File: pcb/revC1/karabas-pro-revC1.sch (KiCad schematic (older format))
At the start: 149 parts, among them CON1 CF-CARD, CON2 SD, CON3 VGA, CON4 Joystick, CON5 Keyboard, CON6 Mouse, CON7 Audio, CON8 5V DC, CON9 MicroSD', J1 Floppy, J2 FPGA JTAG, J3 Floppy, J4 uBus, J5 AVR JTAG, J6 AVR UART, SW1 SW_Push, SW2 SW_Push, SW3 Mode Selector, U1 EP4CE6E22C8N, U10 ESP-12E, U11 TDA1543, U12 AMS1117-3.3, U13 AMS1117-2.5, U14 AMS1117-1.2, U17 74LS06, U18 74LS38, U2 CY62167EV30, U3 M25P16, U4 EPM3128ATC100-5, U5 ATMEGA328-AU, U6 MB8877A, U7 TXB0104PW, U8 TXB0104PW, U9 DS1307Z+, X1 SG-7050CAN, Y1 32768Hz, Y2 16MHz

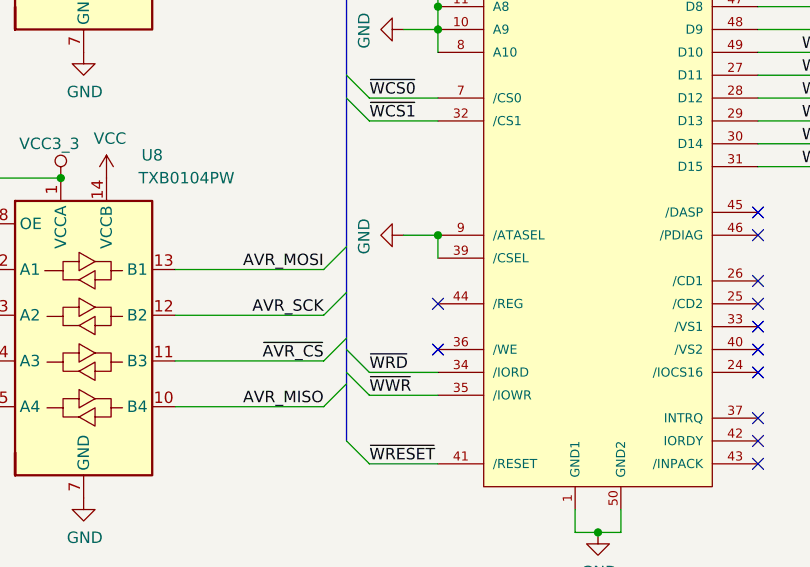
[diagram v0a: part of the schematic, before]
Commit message: Updated rev.C1: added CF card /REG pullup
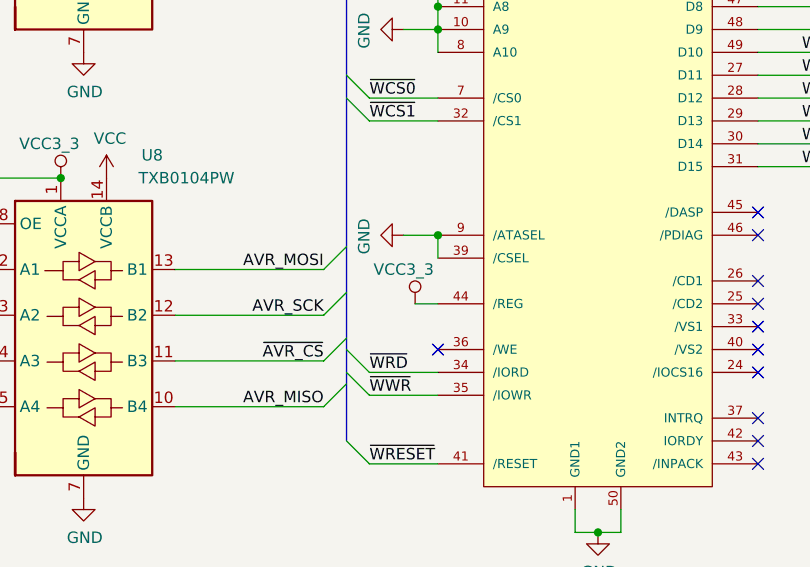
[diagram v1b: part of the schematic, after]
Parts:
- CON1: footprint footprints:TE_1734451-1 -> footprints:TE_1734451-1-LONG
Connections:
- net VCC3_3: now also CON1.44 (/REG)
- no-connect marks 60 -> 59
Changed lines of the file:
@@
 F 0 "CON1" H 9850 11931 50  0000 C CNN
 F 1 "CF-CARD" H 9850 11840 50  0000 C CNN
-F 2 "footprints:TE_1734451-1" H 9880 10300 20  0001 C CNN
+F 2 "footprints:TE_1734451-1-LONG" H 9880 10300 20  0001 C CNN
 F 3 "" H 9850 10150 60  0000 C CNN
 	1    9850 10150
@@
 	9150 10650 9150 10550
 Connection ~ 9150 10550
-NoConn ~ 9150 10850
 NoConn ~ 9150 11050
 Entry Wire Line
@@
 	1    0    0    -1
 $EndComp
-Wire Bus Line
-	14200 10200 14200 11000
-Wire Bus Line
-	14200 700  14200 10200
-Wire Bus Line
-	16000 4950 20350 4950
-Wire Bus Line
-	20350 4950 20350 10200
-Wire Bus Line
-	14200 10200 20350 10200
-Wire Bus Line
-	11050 700  11050 10150
-Wire Bus Line
-	4850 6350 4850 12550
-Wire Bus Line
-	3150 6350 3150 10550
-Wire Bus Line
-	700  6350 700  9700
-Wire Bus Line
-	700  700  6500 700
-Wire Bus Line
-	8750 700  8750 11450
-Wire Bus Line
-	6500 700  6500 11200
-Wire Bus Line
-	4850 6350 5350 6350
-Wire Bus Line
-	3150 6350 4850 6350
-Wire Bus Line
-	700  6350 3150 6350
-Wire Bus Line
-	700  700  700  6350
 Wire Wire Line
 	16550 10750 16950 10750
@@
 	15750 10750 16550 10750
 $Comp
-L vcc33:VCC3_3 #PWR?
+L vcc33:VCC3_3 #PWR0188
 U 1 1 5FD0478B
 P 17850 11550
-F 0 "#PWR?" H 17850 11400 50  0001 C CNN
+F 0 "#PWR0188" H 17850 11400 50  0001 C CNN
 F 1 "VCC3_3" H 17800 11700 50  0000 C CNN
 F 2 "" H 17850 11550 50  0001 C CNN
@@
 $EndComp
 $Comp
-L power:GND #PWR?
+L power:GND #PWR0189
 U 1 1 5FD04E19
 P 17850 11850
-F 0 "#PWR?" H 17850 11600 50  0001 C CNN
+F 0 "#PWR0189" H 17850 11600 50  0001 C CNN
 F 1 "GND" H 17855 11677 50  0000 C CNN
 F 2 "" H 17850 11850 50  0001 C CNN
@@
 	1    0    0    -1
 $EndComp
+$Comp
+L vcc33:VCC3_3 #PWR0190
+U 1 1 5FDAE6BE
+P 9050 10850
+F 0 "#PWR0190" H 9050 10700 50  0001 C CNN
+F 1 "VCC3_3" H 9000 11000 50  0000 C CNN
+F 2 "" H 9050 10850 50  0001 C CNN
+F 3 "" H 9050 10850 50  0001 C CNN
+	1    9050 10850
+	1    0    0    -1
+$EndComp
+Wire Wire Line
+	9050 10850 9150 10850
+Wire Bus Line
+	14200 10200 14200 11000
+Wire Bus Line
+	4850 6350 5350 6350
+Wire Bus Line
+	700  6350 3150 6350
+Wire Bus Line
+	3150 6350 3150 10550
+Wire Bus Line
+	700  6350 700  9700
+Wire Bus Line
+	3150 6350 4850 6350
+Wire Bus Line
+	700  700  700  6350
+Wire Bus Line
+	14200 10200 20350 10200
+Wire Bus Line
+	20350 4950 20350 10200
+Wire Bus Line
+	16000 4950 20350 4950
+Wire Bus Line
+	14200 700  14200 10200
+Wire Bus Line
+	4850 6350 4850 12550
+Wire Bus Line
+	700  700  6500 700
+Wire Bus Line
+	11050 700  11050 10150
+Wire Bus Line
+	6500 700  6500 11200
+Wire Bus Line
+	8750 700  8750 11450
 $EndSCHEMATC

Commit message: Grounded mounting holes and vga connector
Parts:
- CON3: symbol Connector:DB15_Female_HighDensity -> Connector:DB15_Female_HighDensity_MountingHoles
- H1, H2, H3, H4, H5, H6, H7, H8: symbol Mechanical:MountingHole -> Mechanical:MountingHole_Pad
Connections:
- net GND: now also CON3.0, H1.1, H2.1, H3.1, H4.1, H5.1, H6.1, H7.1, H8.1
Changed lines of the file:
@@
 $EndComp
 $Comp
-L Connector:DB15_Female_HighDensity CON3
+L Connector:DB15_Female_HighDensity_MountingHoles CON3
 U 1 1 5F338B53
 P 12650 1900
@@
 $EndComp
 $Comp
-L Mechanical:MountingHole H1
+L Mechanical:MountingHole_Pad H1
 U 1 1 5F34B048
-P 17550 14000
-F 0 "H1" H 17650 14046 50  0000 L CNN
-F 1 "MountingHole" H 17650 13955 50  0000 L CNN
-F 2 "MountingHole:MountingHole_3.5mm_Pad_Via" H 17550 14000 50  0001 C CNN
-F 3 "~" H 17550 14000 50  0001 C CNN
-	1    17550 14000
+P 14850 13950
+F 0 "H1" H 14950 13996 50  0000 L CNN
+F 1 "MountingHole" H 14950 13905 50  0000 L CNN
+F 2 "MountingHole:MountingHole_3.5mm_Pad_Via" H 14850 13950 50  0001 C CNN
+F 3 "~" H 14850 13950 50  0001 C CNN
+	1    14850 13950
 	1    0    0    -1
 $EndComp
 $Comp
-L Mechanical:MountingHole H2
+L Mechanical:MountingHole_Pad H2
 U 1 1 5F34C3F9
-P 17550 14200
-F 0 "H2" H 17650 14246 50  0000 L CNN
-F 1 "MountingHole" H 17650 14155 50  0000 L CNN
-F 2 "MountingHole:MountingHole_3.5mm_Pad_Via" H 17550 14200 50  0001 C CNN
-F 3 "~" H 17550 14200 50  0001 C CNN
-	1    17550 14200
+P 15550 13950
+F 0 "H2" H 15650 13996 50  0000 L CNN
+F 1 "MountingHole" H 15650 13905 50  0000 L CNN
+F 2 "MountingHole:MountingHole_3.5mm_Pad_Via" H 15550 13950 50  0001 C CNN
+F 3 "~" H 15550 13950 50  0001 C CNN
+	1    15550 13950
 	1    0    0    -1
 $EndComp
 $Comp
-L Mechanical:MountingHole H3
+L Mechanical:MountingHole_Pad H3
 U 1 1 5F34C76D
-P 17550 14400
-F 0 "H3" H 17650 14446 50  0000 L CNN
-F 1 "MountingHole" H 17650 14355 50  0000 L CNN
-F 2 "MountingHole:MountingHole_3.5mm_Pad_Via" H 17550 14400 50  0001 C CNN
-F 3 "~" H 17550 14400 50  0001 C CNN
-	1    17550 14400
+P 16250 13950
+F 0 "H3" H 16350 13996 50  0000 L CNN
+F 1 "MountingHole" H 16350 13905 50  0000 L CNN
+F 2 "MountingHole:MountingHole_3.5mm_Pad_Via" H 16250 13950 50  0001 C CNN
+F 3 "~" H 16250 13950 50  0001 C CNN
+	1    16250 13950
 	1    0    0    -1
 $EndComp
 $Comp
-L Mechanical:MountingHole H4
+L Mechanical:MountingHole_Pad H4
 U 1 1 5F34CA0C
-P 17550 14600
-F 0 "H4" H 17650 14646 50  0000 L CNN
-F 1 "MountingHole" H 17650 14555 50  0000 L CNN
-F 2 "MountingHole:MountingHole_3.5mm_Pad_Via" H 17550 14600 50  0001 C CNN
-F 3 "~" H 17550 14600 50  0001 C CNN
-	1    17550 14600
+P 16950 13950
+F 0 "H4" H 17050 13996 50  0000 L CNN
+F 1 "MountingHole" H 17050 13905 50  0000 L CNN
+F 2 "MountingHole:MountingHole_3.5mm_Pad_Via" H 16950 13950 50  0001 C CNN
+F 3 "~" H 16950 13950 50  0001 C CNN
+	1    16950 13950
 	1    0    0    -1
 $EndComp
@@
 $EndComp
 $Comp
-L Mechanical:MountingHole H5
+L Mechanical:MountingHole_Pad H5
 U 1 1 5ED90FCA
-P 17550 14950
-F 0 "H5" H 17650 14996 50  0000 L CNN
-F 1 "MountingHole" H 17650 14905 50  0000 L CNN
-F 2 "MountingHole:MountingHole_3.5mm_Pad_Via" H 17550 14950 50  0001 C CNN
-F 3 "~" H 17550 14950 50  0001 C CNN
-	1    17550 14950
+P 14850 14500
+F 0 "H5" H 14950 14546 50  0000 L CNN
+F 1 "MountingHole" H 14950 14455 50  0000 L CNN
+F 2 "MountingHole:MountingHole_3.5mm_Pad_Via" H 14850 14500 50  0001 C CNN
+F 3 "~" H 14850 14500 50  0001 C CNN
+	1    14850 14500
 	1    0    0    -1
 $EndComp
 $Comp
-L Mechanical:MountingHole H6
+L Mechanical:MountingHole_Pad H6
 U 1 1 5ED90FD4
-P 17550 15150
-F 0 "H6" H 17650 15196 50  0000 L CNN
-F 1 "MountingHole" H 17650 15105 50  0000 L CNN
-F 2 "MountingHole:MountingHole_3.5mm_Pad_Via" H 17550 15150 50  0001 C CNN
-F 3 "~" H 17550 15150 50  0001 C CNN
-	1    17550 15150
+P 15550 14500
+F 0 "H6" H 15650 14546 50  0000 L CNN
+F 1 "MountingHole" H 15650 14455 50  0000 L CNN
+F 2 "MountingHole:MountingHole_3.5mm_Pad_Via" H 15550 14500 50  0001 C CNN
+F 3 "~" H 15550 14500 50  0001 C CNN
+	1    15550 14500
 	1    0    0    -1
 $EndComp
 $Comp
-L Mechanical:MountingHole H7
+L Mechanical:MountingHole_Pad H7
 U 1 1 5ED90FDE
-P 17550 15350
-F 0 "H7" H 17650 15396 50  0000 L CNN
-F 1 "MountingHole" H 17650 15305 50  0000 L CNN
-F 2 "MountingHole:MountingHole_3.5mm_Pad_Via" H 17550 15350 50  0001 C CNN
-F 3 "~" H 17550 15350 50  0001 C CNN
-	1    17550 15350
+P 16250 14500
+F 0 "H7" H 16350 14546 50  0000 L CNN
+F 1 "MountingHole" H 16350 14455 50  0000 L CNN
+F 2 "MountingHole:MountingHole_3.5mm_Pad_Via" H 16250 14500 50  0001 C CNN
+F 3 "~" H 16250 14500 50  0001 C CNN
+	1    16250 14500
 	1    0    0    -1
 $EndComp
 $Comp
-L Mechanical:MountingHole H8
+L Mechanical:MountingHole_Pad H8
 U 1 1 5ED90FE8
-P 17550 15550
-F 0 "H8" H 17650 15596 50  0000 L CNN
-F 1 "MountingHole" H 17650 15505 50  0000 L CNN
-F 2 "MountingHole:MountingHole_3.5mm_Pad_Via" H 17550 15550 50  0001 C CNN
-F 3 "~" H 17550 15550 50  0001 C CNN
-	1    17550 15550
+P 16950 14500
+F 0 "H8" H 17050 14546 50  0000 L CNN
+F 1 "MountingHole" H 17050 14455 50  0000 L CNN
+F 2 "MountingHole:MountingHole_3.5mm_Pad_Via" H 16950 14500 50  0001 C CNN
+F 3 "~" H 16950 14500 50  0001 C CNN
+	1    16950 14500
 	1    0    0    -1
 $EndComp
@@
 Wire Wire Line
 	9050 10850 9150 10850
+$Comp
+L power:GND #PWR0191
+U 1 1 5FE9ECFA
+P 12650 2600
+F 0 "#PWR0191" H 12650 2350 50  0001 C CNN
+F 1 "GND" H 12655 2427 50  0000 C CNN
+F 2 "" H 12650 2600 50  0001 C CNN
+F 3 "" H 12650 2600 50  0001 C CNN
+	1    12650 2600
+	1    0    0    -1
+$EndComp
 Wire Bus Line
 	14200 10200 14200 11000
@@
 Wire Bus Line
 	8750 700  8750 11450
+$Comp
+L power:GND #PWR?
+U 1 1 5FFA1F32
+P 14850 14050
+F 0 "#PWR?" H 14850 13800 50  0001 C CNN
+F 1 "GND" H 14855 13877 50  0000 C CNN
+F 2 "" H 14850 14050 50  0001 C CNN
+F 3 "" H 14850 14050 50  0001 C CNN
+	1    14850 14050
+	1    0    0    -1
+$EndComp
+$Comp
+L power:GND #PWR?
+U 1 1 5FFA5243
+P 15550 14050
+F 0 "#PWR?" H 15550 13800 50  0001 C CNN
+F 1 "GND" H 15555 13877 50  0000 C CNN
+F 2 "" H 15550 14050 50  0001 C CNN
+F 3 "" H 15550 14050 50  0001 C CNN
+	1    15550 14050
+	1    0    0    -1
+$EndComp
+$Comp
+L power:GND #PWR?
+U 1 1 5FFA827A
+P 16250 14050
+F 0 "#PWR?" H 16250 13800 50  0001 C CNN
+F 1 "GND" H 16255 13877 50  0000 C CNN
+F 2 "" H 16250 14050 50  0001 C CNN
+F 3 "" H 16250 14050 50  0001 C CNN
+	1    16250 14050
+	1    0    0    -1
+$EndComp
+$Comp
+L power:GND #PWR?
+U 1 1 5FFAABC3
+P 16950 14050
+F 0 "#PWR?" H 16950 13800 50  0001 C CNN
+F 1 "GND" H 16955 13877 50  0000 C CNN
+F 2 "" H 16950 14050 50  0001 C CNN
+F 3 "" H 16950 14050 50  0001 C CNN
+	1    16950 14050
+	1    0    0    -1
+$EndComp
+$Comp
+L power:GND #PWR?
+U 1 1 5FFAD941
+P 14850 14600
+F 0 "#PWR?" H 14850 14350 50  0001 C CNN
+F 1 "GND" H 14855 14427 50  0000 C CNN
+F 2 "" H 14850 14600 50  0001 C CNN
+F 3 "" H 14850 14600 50  0001 C CNN
+	1    14850 14600
+	1    0    0    -1
+$EndComp
+$Comp
+L power:GND #PWR?
+U 1 1 5FFB1B14
+P 15550 14600
+F 0 "#PWR?" H 15550 14350 50  0001 C CNN
+F 1 "GND" H 15555 14427 50  0000 C CNN
+F 2 "" H 15550 14600 50  0001 C CNN
+F 3 "" H 15550 14600 50  0001 C CNN
+	1    15550 14600
+	1    0    0    -1
+$EndComp
+$Comp
+L power:GND #PWR?
+U 1 1 5FFB51FA
+P 16250 14600
+F 0 "#PWR?" H 16250 14350 50  0001 C CNN
+F 1 "GND" H 16255 14427 50  0000 C CNN
+F 2 "" H 16250 14600 50  0001 C CNN
+F 3 "" H 16250 14600 50  0001 C CNN
+	1    16250 14600
+	1    0    0    -1
+$EndComp
+$Comp
+L power:GND #PWR?
+U 1 1 5FFB8D8E
+P 16950 14600
+F 0 "#PWR?" H 16950 14350 50  0001 C CNN
+F 1 "GND" H 16955 14427 50  0000 C CNN
+F 2 "" H 16950 14600 50  0001 C CNN
+F 3 "" H 16950 14600 50  0001 C CNN
+	1    16950 14600
+	1    0    0    -1
+$EndComp
 $EndSCHEMATC
